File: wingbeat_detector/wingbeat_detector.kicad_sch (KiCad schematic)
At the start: 4 parts, among them J1 USB_C_10137062-00021LF, J2 CONN_UMC_JACK_SMD, U1 UAF42_SMA

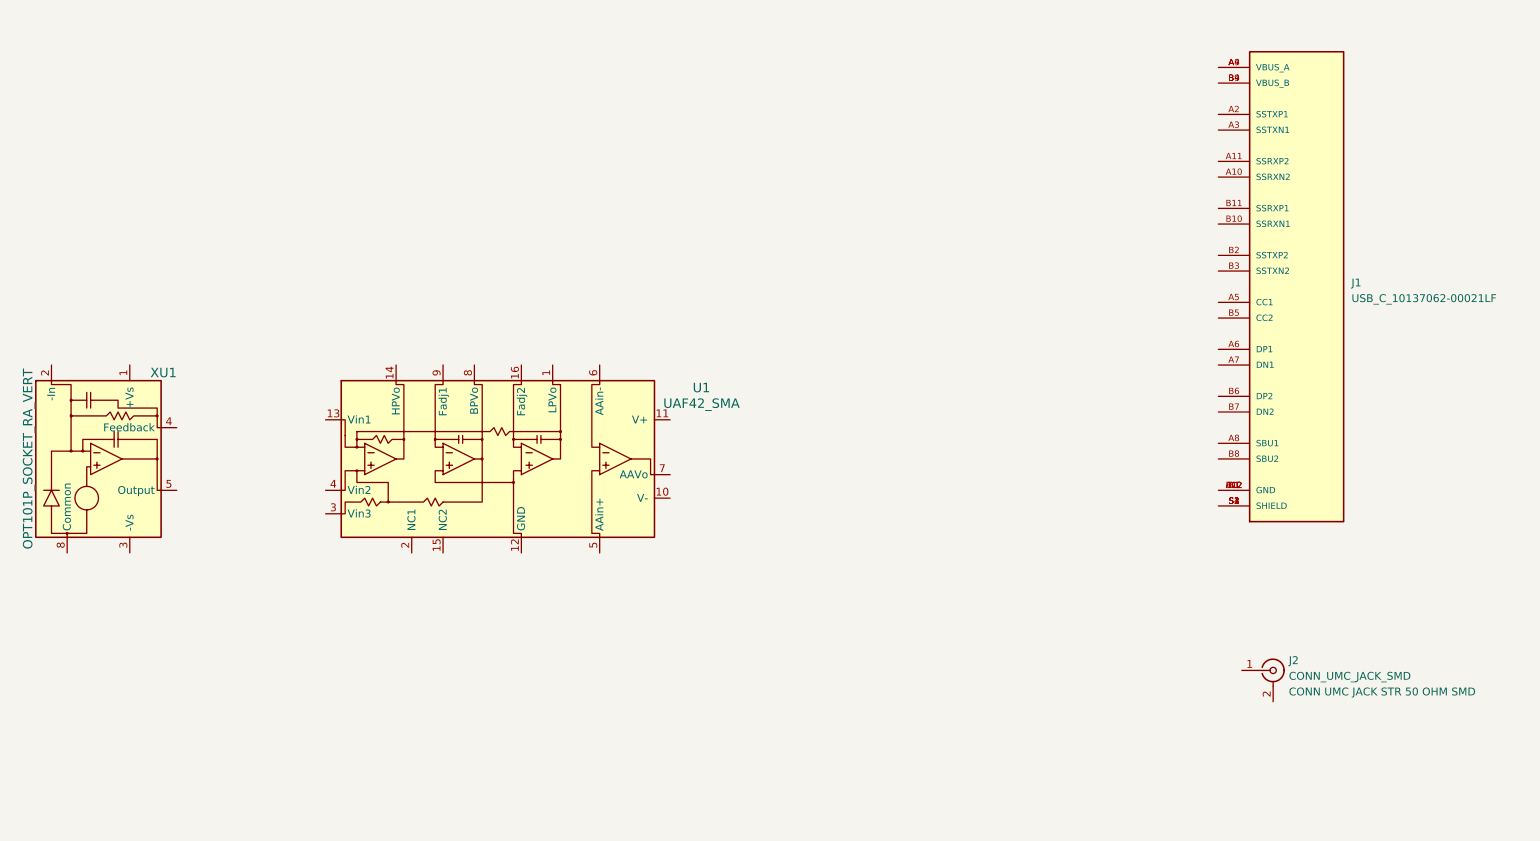
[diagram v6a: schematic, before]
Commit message: Add MAX865
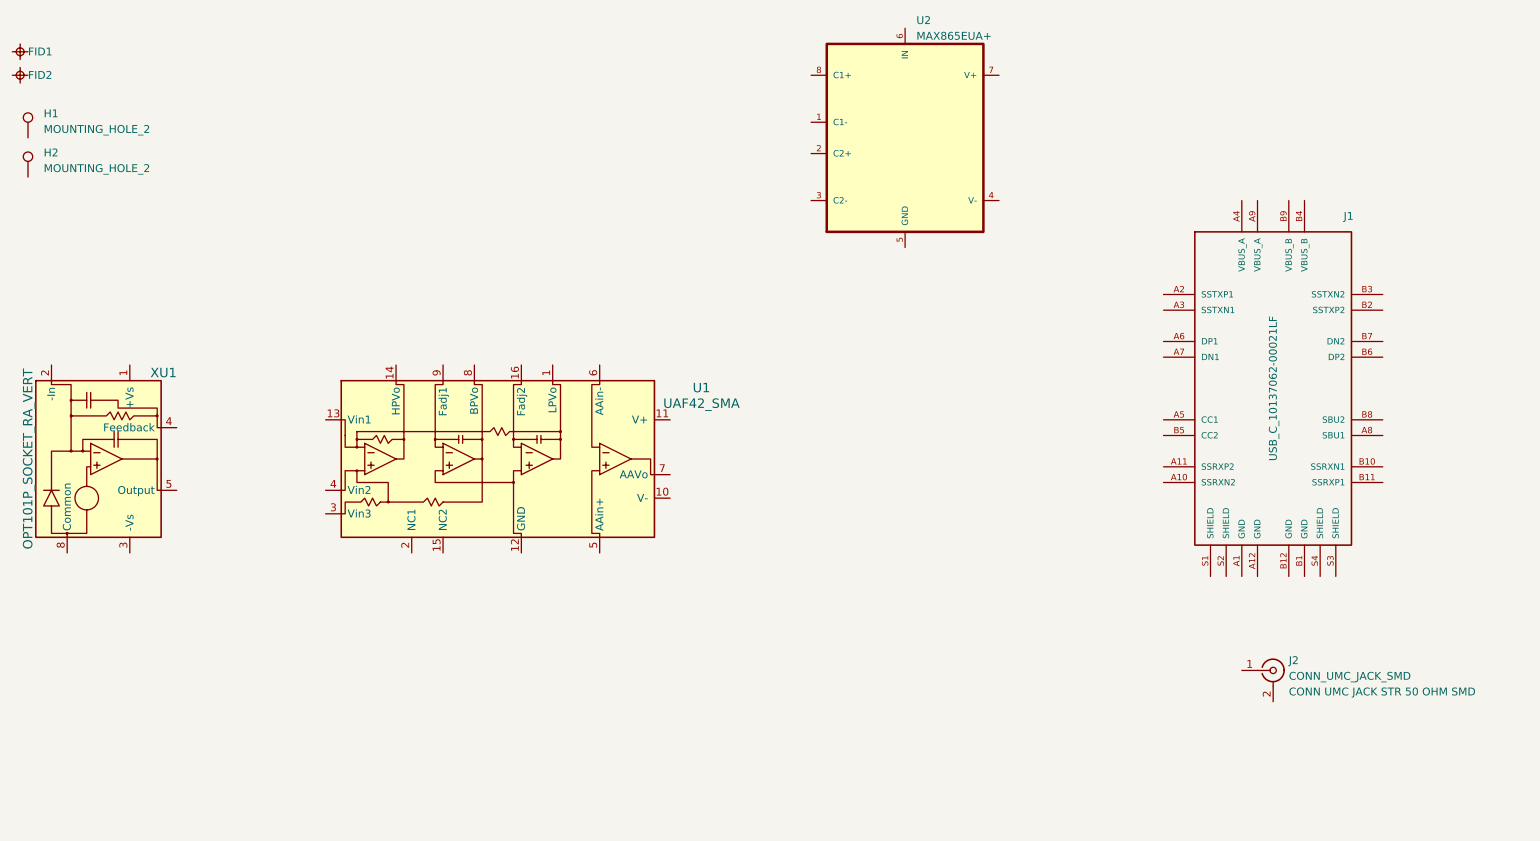
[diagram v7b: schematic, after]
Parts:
- added FID1, FID2: FIDUCIAL_0.5mm_MASK1mm, Janelia:FIDUCIAL_0.5mm_Mask1mm, symbol Janelia:FIDUCIAL_0.5mm_MASK1mm
- added H1, H2: MOUNTING_HOLE_2, Janelia:MOUNTING_HOLE_2, symbol Janelia:MOUNTING_HOLE_2
- added U2: MAX865EUA+, Janelia:SOP65P490X110-8N, symbol Janelia:MAX865EUA+
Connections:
- net at J1.A4 (VBUS_A): no longer J1.A9 (VBUS_A)
- net at J1.B4 (VBUS_B): no longer J1.B9 (VBUS_B)
- now unconnected: J1.A1 (GND), J1.A12 (GND), J1.B1 (GND), J1.B12 (GND), J1.S1 (SHIELD), J1.S2 (SHIELD), J1.S3 (SHIELD), J1.S4 (SHIELD)
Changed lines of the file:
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@@
     (company "Howard Hughes Medical Institute")
   )
+  (symbol (lib_id "Janelia:MAX865EUA+") (at 171.45 38.1 0) (unit 1)
+    (in_bom yes) (on_board yes) (dnp no) (fields_autoplaced)
+    (property "Reference" "U2" (at 173.2789 19.05 0)
+      (effects (font (size 1.27 1.27)) (justify left))
+    )
+    (property "Value" "MAX865EUA+" (at 173.2789 21.59 0)
+      (effects (font (size 1.27 1.27)) (justify left))
+    )
+    (property "Footprint" "Janelia:SOP65P490X110-8N" (at 171.45 -5.08 0)
+      (effects (font (size 1.27 1.27)) (justify bottom) hide)
+    )
+    (property "Datasheet" "" (at 171.45 38.1 0)
+      (effects (font (size 1.27 1.27)) (justify left bottom) hide)
+    )
+    (property "Package" "SOP65P490X110-8N" (at 171.45 1.27 0)
+      (effects (font (size 1.27 1.27)) (justify bottom) hide)
+    )
+    (property "Manufacturer" "Maxim Integrated" (at 171.45 3.81 0)
+      (effects (font (size 1.27 1.27)) (justify bottom) hide)
+    )
+    (property "Manufacturer Part Number" "MAX865EUA+" (at 171.45 -11.43 0)
+      (effects (font (size 1.27 1.27)) hide)
+    )
+    (property "Vendor" "Digi-Key" (at 171.45 5.08 0)
+      (effects (font (size 1.27 1.27)) hide)
+    )
+    (property "Vendor Part Number" "MAX865EUA+-ND" (at 171.45 -8.89 0)
+      (effects (font (size 1.27 1.27)) hide)
+    )
+    (property "Description" "IC REG CHARGE PUMP INV DL 8UMAX" (at 171.45 -2.54 0)
+      (effects (font (size 1.27 1.27)) hide)
+    )
+    (pin "1")
+    (pin "2")
+    (pin "3")
+    (pin "4")
+    (pin "5")
+    (pin "6")
+    (pin "7")
+    (pin "8")
+    (instances
+      (project "wingbeat_detector"
+        (path "/cc457ebc-4af6-4663-b19f-8cb38f061cb4"
+          (reference "U2") (unit 1)
+        )
+      )
+    )
+  )
+  (symbol (lib_id "Janelia:MOUNTING_HOLE_2") (at 29.21 38.1 0) (unit 1)
+    (in_bom yes) (on_board yes) (dnp no) (fields_autoplaced)
+    (property "Reference" "H1" (at 31.75 34.163 0)
+      (effects (font (size 1.27 1.27)) (justify left))
+    )
+    (property "Value" "MOUNTING_HOLE_2" (at 31.75 36.703 0)
+      (effects (font (size 1.27 1.27)) (justify left))
+    )
+    (property "Footprint" "Janelia:MOUNTING_HOLE_2" (at 34.29 38.1 0)
+      (effects (font (size 1.27 1.27)) hide)
+    )
+    (property "Datasheet" "" (at 34.29 38.1 0)
+      (effects (font (size 1.27 1.27)) hide)
+    )
+    (pin "1")
+    (instances
+      (project "wingbeat_detector"
+        (path "/cc457ebc-4af6-4663-b19f-8cb38f061cb4"
+          (reference "H1") (unit 1)
+        )
+      )
+    )
+  )
+  (symbol (lib_id "Janelia:MOUNTING_HOLE_2") (at 29.21 44.45 0) (unit 1)
+    (in_bom yes) (on_board yes) (dnp no) (fields_autoplaced)
+    (property "Reference" "H2" (at 31.75 40.513 0)
+      (effects (font (size 1.27 1.27)) (justify left))
+    )
+    (property "Value" "MOUNTING_HOLE_2" (at 31.75 43.053 0)
+      (effects (font (size 1.27 1.27)) (justify left))
+    )
+    (property "Footprint" "Janelia:MOUNTING_HOLE_2" (at 34.29 44.45 0)
+      (effects (font (size 1.27 1.27)) hide)
+    )
+    (property "Datasheet" "" (at 34.29 44.45 0)
+      (effects (font (size 1.27 1.27)) hide)
+    )
+    (pin "1")
+    (instances
+      (project "wingbeat_detector"
+        (path "/cc457ebc-4af6-4663-b19f-8cb38f061cb4"
+          (reference "H2") (unit 1)
+        )
+      )
+    )
+  )
   (symbol (lib_id "Janelia:CONN_UMC_JACK_SMD") (at 231.14 124.46 0) (unit 1)
     (in_bom yes) (on_board yes) (dnp no) (fields_autoplaced)
@@
     )
   )
-  (symbol (lib_id "Janelia:USB_C_10137062-00021LF") (at 234.95 62.23 0) (unit 1)
-    (in_bom yes) (on_board yes) (dnp no) (fields_autoplaced)
-    (property "Reference" "J1" (at 243.84 61.595 0)
-      (effects (font (size 1.27 1.27)) (justify left))
-    )
-    (property "Value" "USB_C_10137062-00021LF" (at 243.84 64.135 0)
-      (effects (font (size 1.27 1.27)) (justify left))
-    )
-    (property "Footprint" "Janelia:USB_C_Receptacle_Amphenol_10137062-00021LF" (at 234.95 62.23 0)
+  (symbol (lib_id "Janelia:USB_C_10137062-00021LF") (at 231.14 78.74 0) (unit 1)
+    (in_bom yes) (on_board yes) (dnp no)
+    (property "Reference" "J1" (at 242.57 50.8 0)
+      (effects (font (size 1.27 1.27)) (justify left))
+    )
+    (property "Value" "USB_C_10137062-00021LF" (at 231.14 78.74 90)
+      (effects (font (size 1.27 1.27)))
+    )
+    (property "Footprint" "Janelia:USB_C_Receptacle_Amphenol_10137062-00021LF" (at 231.14 78.74 0)
       (effects (font (size 1.27 1.27)) (justify left bottom) hide)
     )
-    (property "Datasheet" "" (at 234.95 62.23 0)
+    (property "Datasheet" "" (at 231.14 78.74 0)
       (effects (font (size 1.27 1.27)) (justify left bottom) hide)
     )
-    (property "Manufacturer" "Amphenol" (at 234.95 62.23 0)
+    (property "Manufacturer" "Amphenol" (at 231.14 78.74 0)
       (effects (font (size 1.27 1.27)) (justify left bottom) hide)
     )
-    (property "Manufacturer Part Number" "10137062-00021LF" (at 234.95 62.23 0)
-      (effects (font (size 1.27 1.27)) hide)
-    )
-    (property "Vendor" "Digi-Key" (at 234.95 62.23 0)
-      (effects (font (size 1.27 1.27)) hide)
-    )
-    (property "Vendor Part Number" "609-6109-1-ND" (at 234.95 62.23 0)
-      (effects (font (size 1.27 1.27)) hide)
-    )
-    (property "Description" "CONN RCP USB3.1 TYPEC 24P SMD RA" (at 234.95 62.23 0)
+    (property "Manufacturer Part Number" "10137062-00021LF" (at 231.14 78.74 0)
+      (effects (font (size 1.27 1.27)) hide)
+    )
+    (property "Vendor" "Digi-Key" (at 231.14 78.74 0)
+      (effects (font (size 1.27 1.27)) hide)
+    )
+    (property "Vendor Part Number" "609-6109-1-ND" (at 231.14 78.74 0)
+      (effects (font (size 1.27 1.27)) hide)
+    )
+    (property "Description" "CONN RCP USB3.1 TYPEC 24P SMD RA" (at 231.14 78.74 0)
       (effects (font (size 1.27 1.27)) hide)
     )
@@
     )
   )
+  (symbol (lib_id "Janelia:FIDUCIAL_0.5mm_MASK1mm") (at 27.94 24.13 0) (unit 1)
+    (in_bom no) (on_board yes) (dnp no)
+    (property "Reference" "FID1" (at 29.21 24.13 0)
+      (effects (font (size 1.27 1.27)) (justify left))
+    )
+    (property "Value" "FIDUCIAL_0.5mm_MASK1mm" (at 27.94 26.416 0)
+      (effects (font (size 1.27 1.27)) hide)
+    )
+    (property "Footprint" "Janelia:FIDUCIAL_0.5mm_Mask1mm" (at 33.02 24.13 0)
+      (effects (font (size 1.27 1.27)) hide)
+    )
+    (property "Datasheet" "" (at 33.02 24.13 0)
+      (effects (font (size 1.27 1.27)) hide)
+    )
+    (instances
+      (project "wingbeat_detector"
+        (path "/cc457ebc-4af6-4663-b19f-8cb38f061cb4"
+          (reference "FID1") (unit 1)
+        )
+      )
+    )
+  )
   (symbol (lib_id "Janelia:UAF42_SMA") (at 105.41 90.17 0) (unit 1)
     (in_bom yes) (on_board yes) (dnp no) (fields_autoplaced)
@@
         )
       )
+    )
+  )
+  (symbol (lib_id "Janelia:FIDUCIAL_0.5mm_MASK1mm") (at 27.94 27.94 0) (unit 1)
+    (in_bom no) (on_board yes) (dnp no)
+    (property "Reference" "FID2" (at 29.21 27.94 0)
+      (effects (font (size 1.27 1.27)) (justify left))
+    )
+    (property "Value" "FIDUCIAL_0.5mm_MASK1mm" (at 27.94 30.226 0)
+      (effects (font (size 1.27 1.27)) hide)
+    )
+    (property "Footprint" "Janelia:FIDUCIAL_0.5mm_Mask1mm" (at 33.02 27.94 0)
+      (effects (font (size 1.27 1.27)) hide)
+    )
+    (property "Datasheet" "" (at 33.02 27.94 0)
+      (effects (font (size 1.27 1.27)) hide)
+    )
+    (instances
+      (project "wingbeat_detector"
+        (path "/cc457ebc-4af6-4663-b19f-8cb38f061cb4"
+          (reference "FID2") (unit 1)
+        )
+      )
